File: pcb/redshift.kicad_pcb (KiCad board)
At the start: 4 copper layers, 45 x 65 mm, 11 parts, among them IC1 LPC5516JEV98, J1 USB_C_Receptacle_USB2.0, SW1 SW_SPDT, SW2 SW_SPDT, SW4 SW_SPDT, U1 PMW3389DM‐T3QU

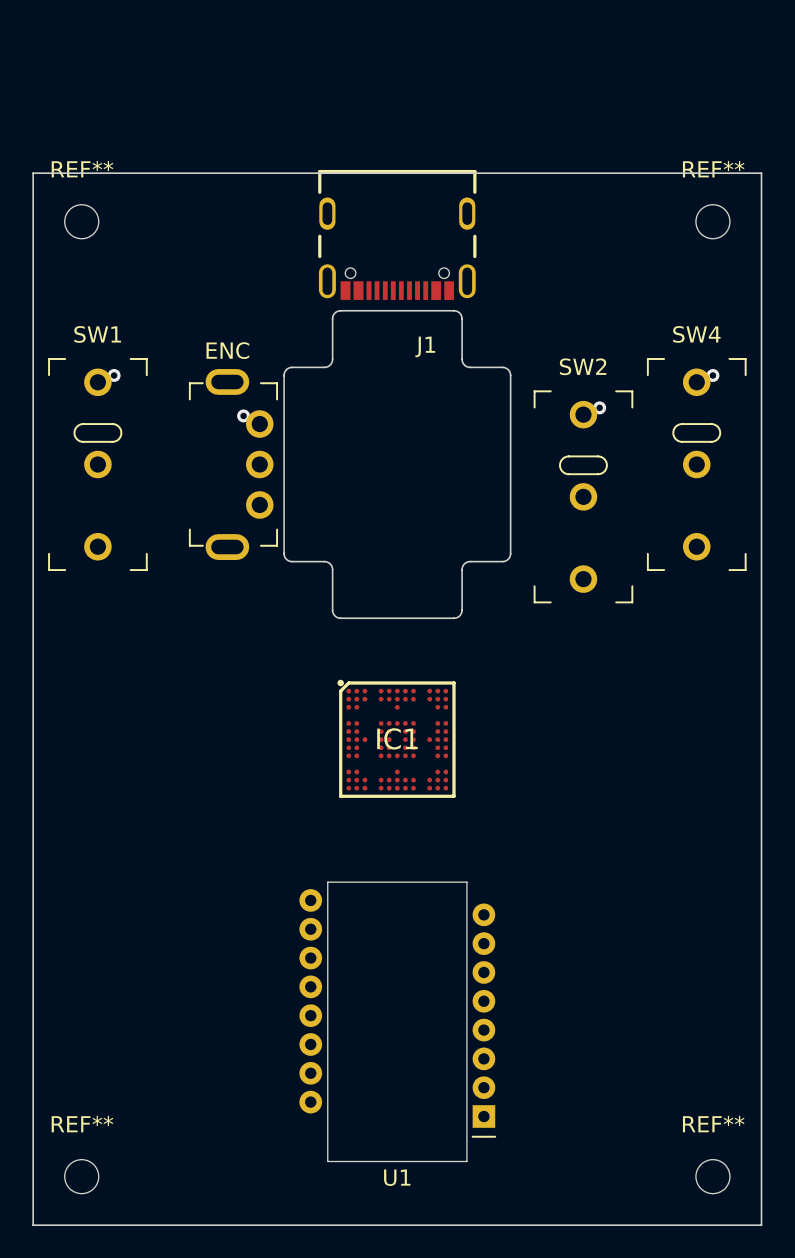
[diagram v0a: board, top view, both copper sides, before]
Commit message: add USB and some power wires
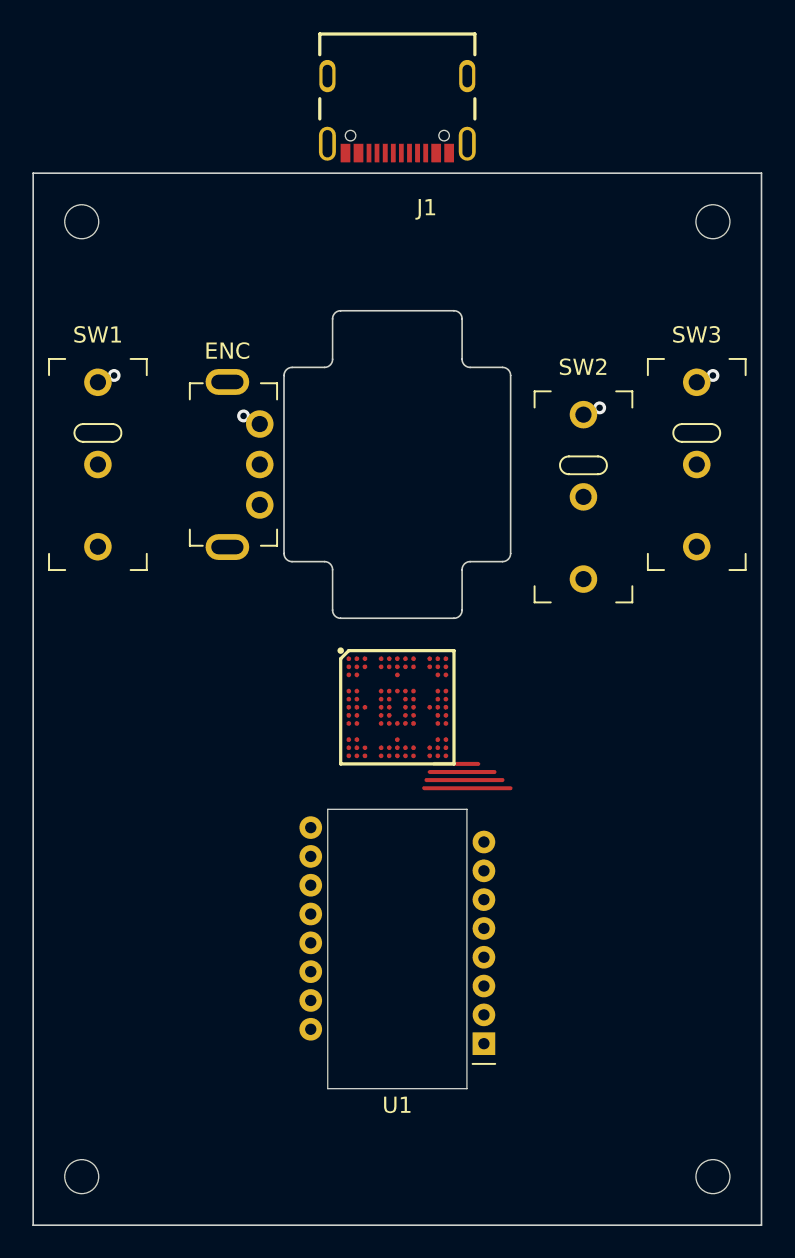
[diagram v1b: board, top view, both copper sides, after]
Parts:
- moved J1 8.50 mm to (137.5, 54.0)
- moved U1 4.50 mm to (142.8, 113.8)
- moved IC1 2.00 mm to (137.5, 93.0)
- renumbered SW4 to SW3
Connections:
- IC1 pad B13: unconnected-(IC1-PadB13) -> /VSS
- IC1 pad B5: unconnected-(IC1-PadB5) -> /VSS
- IC1 pad B9: unconnected-(IC1-PadB9) -> /VSS
- IC1 pad H2: unconnected-(IC1-PadH2) -> /VSS
- IC1 pad M6: unconnected-(IC1-PadM6) -> /D+
- IC1 pad N6: unconnected-(IC1-PadN6) -> /D-
- SW1 pad 2: unconnected-(SW1-Pad2) -> /SW1_L_NO
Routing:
- net unconnected-(IC1-PadN7): track 0.00 -> 5.34 mm
- net unconnected-(IC1-PadN8): track 0.00 -> 4.71 mm
- net unconnected-(IC1-PadN9): track 0.00 -> 4.00 mm
- net unconnected-(IC1-PadN11): track 0.00 -> 2.71 mm

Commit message: route USB and power lines, fix ESD chip
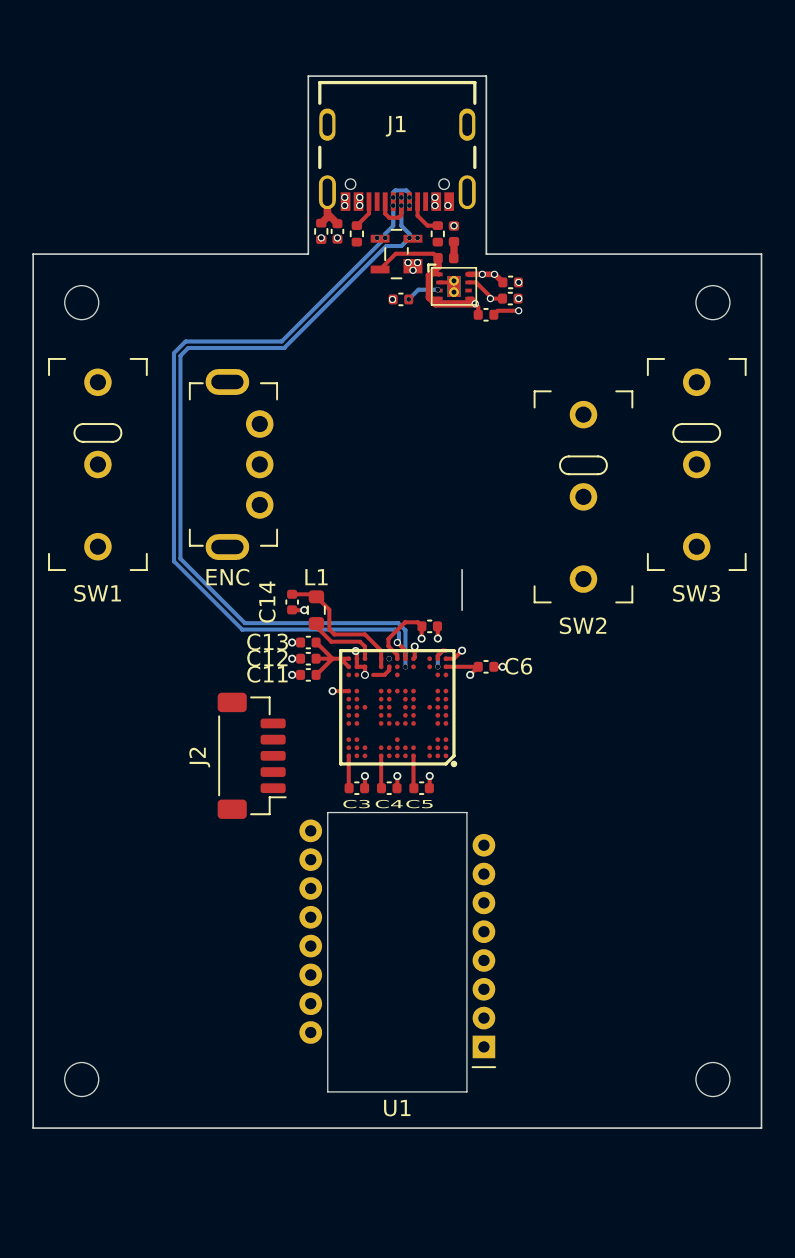
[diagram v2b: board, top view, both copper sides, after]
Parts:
- added C1: 100nF, Capacitor_SMD:C_0402_1005Metric, F.Cu at (133.8, 63.6)
- added C10: 0.1uF, Capacitor_SMD:C_0402_1005Metric, F.Cu at (137.7, 67.8)
- added C11: 22uF, Capacitor_SMD:C_0402_1005Metric, F.Cu at (132.0, 91.0)
- added C12: 100nF, Capacitor_SMD:C_0402_1005Metric, F.Cu at (132.0, 90.0)
- added C13: 47pF, Capacitor_SMD:C_0402_1005Metric, F.Cu at (132.0, 89.0)
- added C14: 22uF, Capacitor_SMD:C_0402_1005Metric, F.Cu at (131.0, 86.5)
- added C2: 2.2uF, Capacitor_SMD:C_0402_1005Metric, F.Cu at (143.0, 68.8)
- added C3: 100nF, Capacitor_SMD:C_0402_1005Metric, F.Cu at (135.0, 98.0)
- added C4: 100nF, Capacitor_SMD:C_0402_1005Metric, F.Cu at (137.0, 98.0)
- added C5: 100nF, Capacitor_SMD:C_0402_1005Metric, F.Cu at (139.0, 98.0)
- added C6: 100nF, Capacitor_SMD:C_0402_1005Metric, F.Cu at (143.0, 90.5)
- added C7: 2.2uF, Capacitor_SMD:C_0402_1005Metric, F.Cu at (144.5, 67.8)
- added C8: 2.2uF, Capacitor_SMD:C_0402_1005Metric, F.Cu at (144.5, 66.8)
- added C9: 100nF, Capacitor_SMD:C_0402_1005Metric, F.Cu at (139.5, 88.0)
- added D1: PRTR5V0U2X, footprints:BF994S, F.Cu at (137.5, 65.0)
- added F1: 500mA, Fuse:Fuse_0402_1005Metric, F.Cu at (141.0, 63.8)
- added FB1: ~, Inductor_SMD:L_0402_1005Metric, F.Cu at (140.5, 65.2)
- added J2: Side, Connector_JST:JST_SH_BM05B-SRSS-TB_1x05-1MP_P1.00mm_Vertical, F.Cu at (128.5, 96.0)
- added L1: 4u7H, Resistor_SMD:R_0603_1608Metric, F.Cu at (132.5, 87.0)
- added R1: 100k, Resistor_SMD:R_0402_1005Metric, F.Cu at (132.8, 63.6)
- added R2: 5.1k, Resistor_SMD:R_0402_1005Metric, F.Cu at (140.0, 63.8)
- added R3: 5.1k, Resistor_SMD:R_0402_1005Metric, F.Cu at (135.0, 63.8)
- added U2: MIC5350-SGYMT-TR, Package_DFN_QFN:Micrel_MLF-8-1EP_2x2mm_P0.5mm_EP0.8x1.3mm_ThermalVias, F.Cu at (141.0, 67.0)
- U1: value PMW3389DM‐T3QU -> PAW 3399
- moved REF** 6.00 mm to (157.0, 116.0)
- moved REF** 6.00 mm to (118.0, 116.0)
- moved REF** 5.00 mm to (157.0, 68.0)
- moved REF** 5.00 mm to (118.0, 68.0)
- moved J1 3.00 mm to (137.5, 57.0)
- moved U1 0.20 mm to (142.8, 114.0)
- turned IC1 to 180 degrees
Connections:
- IC1 pad A11: unconnected-(IC1-PadA11) -> /SW4_NO
- IC1 pad A12: unconnected-(IC1-PadA12) -> /SW4_NC
- IC1 pad A13: unconnected-(IC1-PadA13) -> +3V3
- IC1 pad A5: unconnected-(IC1-PadA5) -> +3V3
- IC1 pad A9: unconnected-(IC1-PadA9) -> +3V3
- IC1 pad B13: /VSS -> GND
- IC1 pad B5: /VSS -> GND
- IC1 pad B9: /VSS -> GND
- IC1 pad C12: unconnected-(IC1-PadC12) -> /SW5_NO
- IC1 pad C13: unconnected-(IC1-PadC13) -> /SW5_NC
- IC1 pad C7: unconnected-(IC1-PadC7) -> /FC6_MISO
- IC1 pad F1: unconnected-(IC1-PadF1) -> /FC6_MOSI
- IC1 pad F2: unconnected-(IC1-PadF2) -> /FC6_SCK
- IC1 pad F9: unconnected-(IC1-PadF9) -> /USB1_LED
- IC1 pad G12: unconnected-(IC1-PadG12) -> Net-(IC1-PadG12)
- IC1 pad G13: unconnected-(IC1-PadG13) -> Net-(IC1-PadG12)
- IC1 pad H2: /VSS -> unconnected-(IC1-PadH2)
- IC1 pad J13: unconnected-(IC1-PadJ13) -> GND
- IC1 pad J6: unconnected-(IC1-PadJ6) -> /RESET
- IC1 pad L2: unconnected-(IC1-PadL2) -> /FC6_CS1
- IC1 pad M1: unconnected-(IC1-PadM1) -> +3V3
- IC1 pad M11: unconnected-(IC1-PadM11) -> GND
- IC1 pad M12: unconnected-(IC1-PadM12) -> GND
- IC1 pad M13: unconnected-(IC1-PadM13) -> /PMU
- IC1 pad M2: unconnected-(IC1-PadM2) -> /SW2_M_NC
- IC1 pad M3: unconnected-(IC1-PadM3) -> /XTAL-
- IC1 pad M6: /D+ -> /USB_D+
- IC1 pad M7: unconnected-(IC1-PadM7) -> Net-(IC1-PadM7)
- IC1 pad M8: unconnected-(IC1-PadM8) -> Net-(IC1-PadM7)
- IC1 pad M9: unconnected-(IC1-PadM9) -> /1v2
- IC1 pad N1: unconnected-(IC1-PadN1) -> GND
- IC1 pad N11: unconnected-(IC1-PadN11) -> /_1v2
- IC1 pad N12: unconnected-(IC1-PadN12) -> GND
- IC1 pad N13: unconnected-(IC1-PadN13) -> /PMU
- IC1 pad N2: unconnected-(IC1-PadN2) -> /SW2_M_NO
- IC1 pad N3: unconnected-(IC1-PadN3) -> /XTAL+
- IC1 pad N5: unconnected-(IC1-PadN5) -> GND
- IC1 pad N6: /D- -> /USB_D-
- IC1 pad N7: unconnected-(IC1-PadN7) -> +3V3
- IC1 pad N8: unconnected-(IC1-PadN8) -> +5V
- IC1 pad N9: unconnected-(IC1-PadN9) -> /1v2
- J1 pad A5: unconnected-(J1-PadA5) -> Net-(J1-PadA5)
- J1 pad A6: unconnected-(J1-PadA6) -> /USB_D+
- J1 pad A7: unconnected-(J1-PadA7) -> /USB_D-
- J1 pad B5: unconnected-(J1-PadB5) -> Net-(J1-PadB5)
- J1 pad B6: unconnected-(J1-PadB6) -> /USB_D+
- J1 pad B7: unconnected-(J1-PadB7) -> /USB_D-
- J1 pad S1: unconnected-(J1-PadS1) -> /SH
- SW1 pad 3: unconnected-(SW1-Pad3) -> /SW1_L_NC
- SW2 pad 2: unconnected-(SW2-Pad2) -> /SW2_M_NO
- SW2 pad 3: unconnected-(SW2-Pad3) -> /SW2_M_NC
- SW3 pad 2: unconnected-(SW3-Pad2) -> /SW3_R_NO
- SW3 pad 3: unconnected-(SW3-Pad3) -> /SW3_R_NC
- U1 pad 10: unconnected-(U1-Pad10) -> /FC6_SCK
- U1 pad 11: unconnected-(U1-Pad11) -> /FC6_MOSI
- U1 pad 12: unconnected-(U1-Pad12) -> /FC6_MISO
- U1 pad 13: unconnected-(U1-Pad13) -> /FC6_CS1
- U1 pad 4: unconnected-(U1-Pad4) -> +1V8
- U1 pad 5: unconnected-(U1-Pad5) -> +3V3
- U1 pad 8: unconnected-(U1-Pad8) -> GND
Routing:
- net /USB_D+: track 0.00 -> 53.6 mm, vias 0 -> 5
- net /USB_D-: track 0.00 -> 51.8 mm, vias 0 -> 7
- net +1V8: track 0.00 -> 47.0 mm, vias 0 -> 1
- net +5V: track 0.00 -> 45.0 mm, vias 0 -> 2
- net /SH: track 0.00 -> 21.3 mm
- net +3V3: track 0.00 -> 17.4 mm, vias 0 -> 7
- net GND: track 0.00 -> 12.0 mm, vias 4 -> 23
- net /VBUS_: track 0.00 -> 8.95 mm, vias 0 -> 5
- net /1v2: track 0.00 -> 8.65 mm
- net /PMU: track 0.00 -> 5.60 mm
- net unconnected-(IC1-PadN7): track 5.34 -> 0.00 mm
- net unconnected-(IC1-PadN8): track 4.71 -> 0.00 mm
- net /_1v2: track 0.00 -> 4.46 mm
- net unconnected-(IC1-PadN9): track 4.00 -> 0.00 mm
- net unconnected-(IC1-PadN11): track 2.71 -> 0.00 mm
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- added copper zone on In2.Cu, net +3V3
- removed copper zone on In2.Cu, net (none)
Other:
- outline, holes or cut-outs redrawn

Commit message: add trace header and LEDs
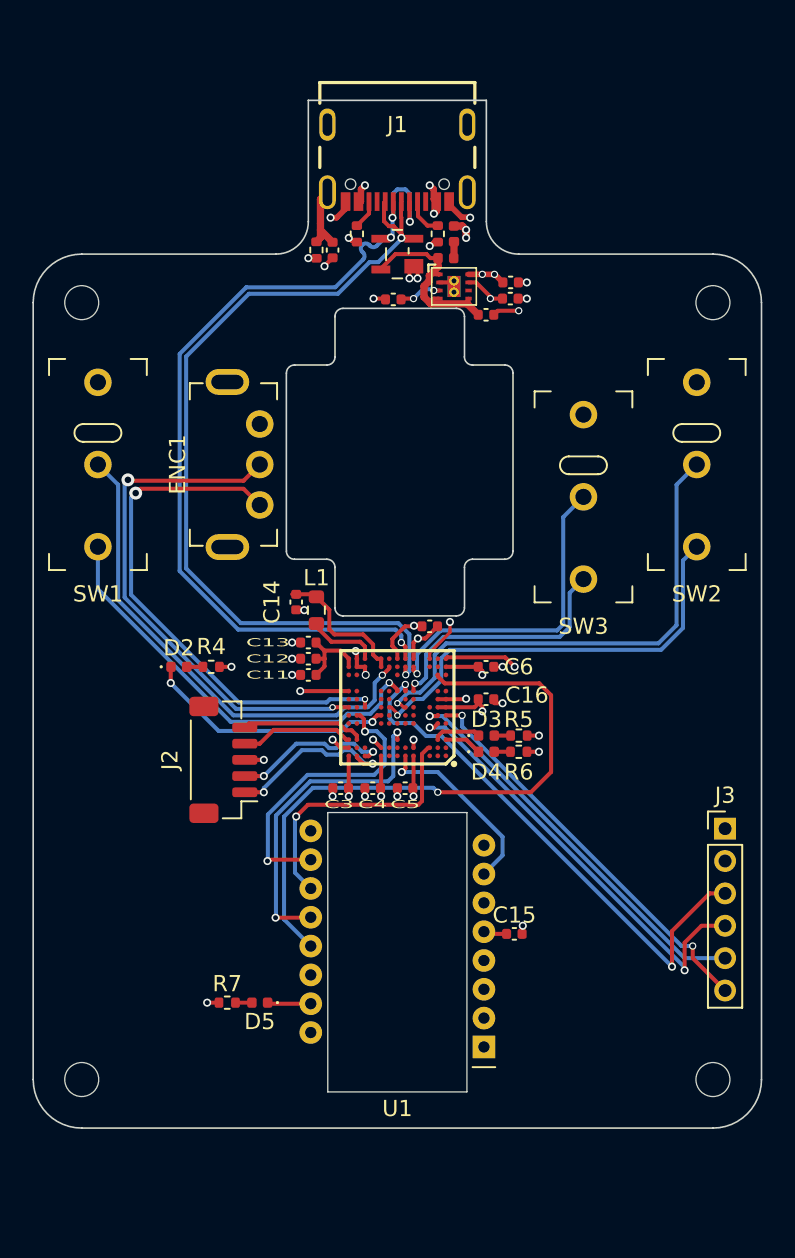
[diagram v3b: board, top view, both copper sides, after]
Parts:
- removed ENC: Rotary_Encoder, openinput:RotaryEncoder_Horizontal
- added C15: 100nF, Capacitor_SMD:C_0402_1005Metric, F.Cu at (144.7, 107.0)
- added C16: 100nF, Capacitor_SMD:C_0402_1005Metric, F.Cu at (143.0, 92.5)
- added D2: RED, LED_SMD:LED_0402_1005Metric, F.Cu at (124.0, 90.5)
- added D3: AMBER, LED_SMD:LED_0402_1005Metric, F.Cu at (143.0, 94.8)
- added D4: GREEN, LED_SMD:LED_0402_1005Metric, F.Cu at (143.0, 95.8)
- added D5: RED, LED_SMD:LED_0402_1005Metric, F.Cu at (129.0, 111.2)
- added ENC1: Rotary_Encoder, openinput:RotaryEncoder_Horizontal, F.Cu at (129.0, 78.0)
- added J3: Conn_01x06_Female, Connector_PinHeader_2.00mm:PinHeader_1x06_P2.00mm_Vertical, F.Cu at (157.8, 100.5)
- added R4: 100R, Resistor_SMD:R_0402_1005Metric, F.Cu at (126.0, 90.5)
- added R5: 100R, Resistor_SMD:R_0402_1005Metric, F.Cu at (145.0, 94.8)
- added R6: 100R, Resistor_SMD:R_0402_1005Metric, F.Cu at (145.0, 95.8)
- added R7: 100R, Resistor_SMD:R_0402_1005Metric, F.Cu at (127.0, 111.2)
- SW3: renamed from SW2; value SW_SPDT -> SW_SPD
- moved J2 1.77 mm to (126.8, 96.2)
- moved C1 1.19 mm to (133.5, 64.8)
- moved R1 1.19 mm to (132.5, 64.8)
- moved C4 1.02 mm to (136.0, 98.0), turned to 180 degrees
- moved C5 1.02 mm to (138.0, 98.0), turned to 180 degrees
- moved C3 1.00 mm to (134.0, 98.0), turned to 180 degrees
- moved C10 0.47 mm to (137.2, 67.8)
- moved C14 0.25 mm to (131.2, 86.5)
- renumbered SW3 to SW2
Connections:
- IC1 pad A11: /SW4_NO -> /SW4_NC
- IC1 pad A12: /SW4_NC -> /SW4_NO
- IC1 pad A6: unconnected-(IC1-PadA6) -> /SNSR_RST
- IC1 pad B3: unconnected-(IC1-PadB3) -> /FC6_MOSI
- IC1 pad C1: unconnected-(IC1-PadC1) -> /USER_LED
- IC1 pad C2: unconnected-(IC1-PadC2) -> /FAULT_LED
- IC1 pad E2: unconnected-(IC1-PadE2) -> /SWDIO
- IC1 pad F1: /FC6_MOSI -> /SWCLK
- IC1 pad F12: unconnected-(IC1-PadF12) -> /FC6_SCK
- IC1 pad F2: /FC6_SCK -> /SWO
- IC1 pad G1: unconnected-(IC1-PadG1) -> +3V3
- IC1 pad G11: unconnected-(IC1-PadG11) -> /ENC_A
- IC1 pad G12: Net-(IC1-PadG12) -> unconnected-(IC1-PadG12)
- IC1 pad G13: Net-(IC1-PadG12) -> /ENC_B
- IC1 pad G2: unconnected-(IC1-PadG2) -> +3V3
- IC1 pad G6: unconnected-(IC1-PadG6) -> /SW2_R_NO
- IC1 pad G8: unconnected-(IC1-PadG8) -> /SW2_R_NC
- IC1 pad H1: unconnected-(IC1-PadH1) -> GND
- IC1 pad H2: unconnected-(IC1-PadH2) -> GND
- IC1 pad J5: unconnected-(IC1-PadJ5) -> /SW3_M_NC
- IC1 pad J7: unconnected-(IC1-PadJ7) -> /SW1_L_NC
- IC1 pad M2: /SW2_M_NC -> unconnected-(IC1-PadM2)
- IC1 pad M5: unconnected-(IC1-PadM5) -> /SW3_M_NO
- IC1 pad M7: Net-(IC1-PadM7) -> unconnected-(IC1-PadM7)
- IC1 pad M8: Net-(IC1-PadM7) -> /SW1_L_NO
- IC1 pad N2: /SW2_M_NO -> unconnected-(IC1-PadN2)
- IC1 pad N3: /XTAL+ -> GND
- IC1 pad N8: +5V -> unconnected-(IC1-PadN8)
- SW2 pad 2: /SW3_R_NO -> /SW2_R_NO
- SW2 pad 3: /SW3_R_NC -> /SW2_R_NC
- SW3 pad 2: /SW2_M_NO -> /SW3_M_NO
- SW3 pad 3: /SW2_M_NC -> /SW3_M_NC
- U1 pad 15: unconnected-(U1-Pad15) -> /SNSR_LED
- U1 pad 7: unconnected-(U1-Pad7) -> /SNSR_RST
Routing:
- net /VBUS_: track 8.95 -> 65.3 mm
- net /FC6_CS1: track 0.00 -> 38.9 mm, vias 0 -> 1
- net /RESET: track 0.00 -> 33.2 mm, vias 0 -> 2
- net /ENC_B: track 0.00 -> 32.7 mm, vias 0 -> 2
- net /ENC_A: track 0.00 -> 32.4 mm, vias 0 -> 2
- net +5V: track 45.0 -> 12.8 mm, vias 2 -> 0
- net /SW2_R_NO: track 0.00 -> 31.1 mm, vias 0 -> 1
- net /SW1_L_NO: track 0.00 -> 30.5 mm, vias 0 -> 1
- net /SWDIO: track 0.00 -> 27.0 mm, vias 0 -> 2
- net /SW2_R_NC: track 0.00 -> 26.8 mm, vias 0 -> 1
- net /SW1_L_NC: track 0.00 -> 26.2 mm, vias 0 -> 1
- net /SWCLK: track 0.00 -> 25.0 mm, vias 0 -> 2
- net /SWO: track 0.00 -> 25.0 mm, vias 0 -> 1
- net GND: track 12.0 -> 34.6 mm, vias 23 -> 30
- net /FC6_MISO: track 0.00 -> 20.0 mm, vias 0 -> 2
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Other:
- board size 45 x 65 mm -> 45 x 63.5 mm
